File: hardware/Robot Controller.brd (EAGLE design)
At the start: 52.4 x 48.9 mm, 18 parts

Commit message: routing
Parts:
- moved R2 29.7 mm to (82.5, 59.7), turned to 0 degrees
- moved R1 5.85 mm to (82.5, 63.5), turned to 180 degrees
- moved R3 4.96 mm to (57.8, 49.5), turned to 0 degrees
- moved JP1 2.54 mm to (90.8, 43.2)
- moved SN74AHCU04N 1.42 mm to (55.9, 36.8)
- moved ATTINY 1.42 mm to (68.6, 40.6)
- moved JP3 1.27 mm to (55.9, 61.6)
- moved JP4 1.27 mm to (69.2, 61.6)
- moved JP6 1.27 mm to (47.0, 54.6)
- moved H1 1.27 mm to (47.0, 61.0)
- moved L293D 1.27 mm to (81.3, 38.1)
- moved LED1 1.27 mm to (60.3, 55.9)
- moved LED3 1.27 mm to (72.4, 55.9)
- moved S1 1.27 mm to (81.3, 53.3)
- moved LED2 0.63 mm to (48.3, 32.4)
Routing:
- net N$17: track 18.1 -> 74.1 mm, vias 0 -> 2
- net N$8: track 36.7 -> 71.3 mm, vias 0 -> 2
- net VCC: track 80.3 -> 113.3 mm, vias 0 -> 2
- net N$21: track 11.4 -> 36.4 mm, vias 0 -> 1
- net N$9: track 34.0 -> 55.9 mm, vias 0 -> 3
- net N$22: track 64.3 -> 80.9 mm, vias 0 -> 1
- net N$14: track 16.5 -> 32.2 mm, vias 2 -> 0
- net N$11: track 55.7 -> 46.0 mm, vias 3 -> 2
- net N$30: track 25.2 -> 34.5 mm
- net N$6: track 45.7 -> 53.4 mm, vias 0 -> 1
- net N$2: track 25.0 -> 31.6 mm, vias 0 -> 1
- net N$20: track 48.2 -> 54.3 mm, vias 1 -> 2
- net N$13: track 26.7 -> 32.3 mm, vias 1 -> 2
- net N$19: track 37.1 -> 32.0 mm
- net N$15: track 19.3 -> 24.3 mm
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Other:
- board size 52.4 x 48.9 mm -> 51.7 x 47.6 mm
- board text added: "1. A robot may not injure a human being or, through inaction, allow a human being to come to harm. 2. A robot must obey the orders given to it by human beings, except where such orders would conflict with the First Law. 3. A robot must protect its own existence as long as such p rotection does not conflict with the First or Second Laws."

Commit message: tighten up PCB
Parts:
- removed S1: (no value), switch-omron:B3F-10XX
- added JP7: (no value), pinhead:1X08
- JP8: device pinhead:1X10 -> pinhead:1X02
- moved JP2 36.1 mm to (79.4, 57.1), turned to 0 degrees
- moved JP8 34.7 mm to (77.5, 50.8), turned to 180 degrees
- moved R2 31.5 mm to (52.7, 49.5), turned to 90 degrees
- moved R1 29.5 mm to (56.5, 49.5), turned to 270 degrees
- moved H1 17.2 mm to (46.4, 43.8)
- moved JP3 9.38 mm to (47.6, 57.1)
- moved JP4 7.24 mm to (63.5, 57.1)
- moved JP6 3.86 mm to (46.4, 50.8), turned to 0 degrees
- moved LED1 3.59 mm to (57.8, 58.4), turned to 90 degrees
- moved JP5 2.84 mm to (78.7, 22.2)
- moved LED3 2.84 mm to (73.7, 58.4), turned to 90 degrees
- moved R3 2.54 mm to (60.3, 49.5), turned to 90 degrees
- moved JP1 2.54 mm to (90.8, 40.6)
- moved LED2 0.90 mm to (48.9, 33.0), turned to 90 degrees
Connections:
- net GND: now also JP8.2; no longer JP8.10, S1.2
- net N$23: now also JP7.8; no longer JP8.8
- net N$24: now also JP7.7; no longer JP8.7
- net N$25: now also JP7.6; no longer JP8.6
- net N$26: now also JP7.5; no longer JP8.5
- net N$27: now also JP7.4; no longer JP8.4
- net N$28: now also JP7.1; no longer JP8.1
- net N$29: now also JP7.2; no longer JP8.2
- net N$30: now also JP7.3; no longer JP8.3
- net N$31: now also JP8.1; no longer S1.3
- net VCC: no longer JP8.9
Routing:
- net N$8: track 71.3 -> 18.2 mm, vias 2 -> 0
- net N$17: track 74.1 -> 31.2 mm, vias 2 -> 0
- net N$22: track 80.9 -> 40.2 mm, vias 1 -> 2
- net VCC: track 113.3 -> 74.3 mm, vias 2 -> 1
- net N$9: track 55.9 -> 25.2 mm, vias 3 -> 0
- net N$3: track 35.2 -> 6.60 mm, vias 2 -> 0
- net N$21: track 36.4 -> 10.6 mm
- net N$20: track 54.3 -> 35.9 mm, vias 2 -> 0
- net N$19: track 32.0 -> 50.2 mm, vias 0 -> 2
- net GND: track 155.4 -> 139.8 mm, vias 4 -> 0
- net N$10: track 68.7 -> 54.3 mm, vias 2 -> 1
- net N$23: track 55.3 -> 42.7 mm, vias 2 -> 1
- net N$30: track 34.5 -> 23.8 mm
- net N$14: track 32.2 -> 21.8 mm
- net N$6: track 53.4 -> 43.1 mm, vias 1 -> 0
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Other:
- board size 51.7 x 47.6 mm -> 51.7 x 41.3 mm
- board text added: "L1"
- board text added: "RST"
- board text added: "robot core rev 0.1"
- board text removed: "1. A robot may not injure a human being or, through inaction, allow a human being to come to harm. 2. A robot must obey the orders given to it by human beings, except where such orders would conflict with the First Law. 3. A robot must protect its own existence as long as such p rotection does not conflict with the First or Second Laws."
- board text removed: "robot core"

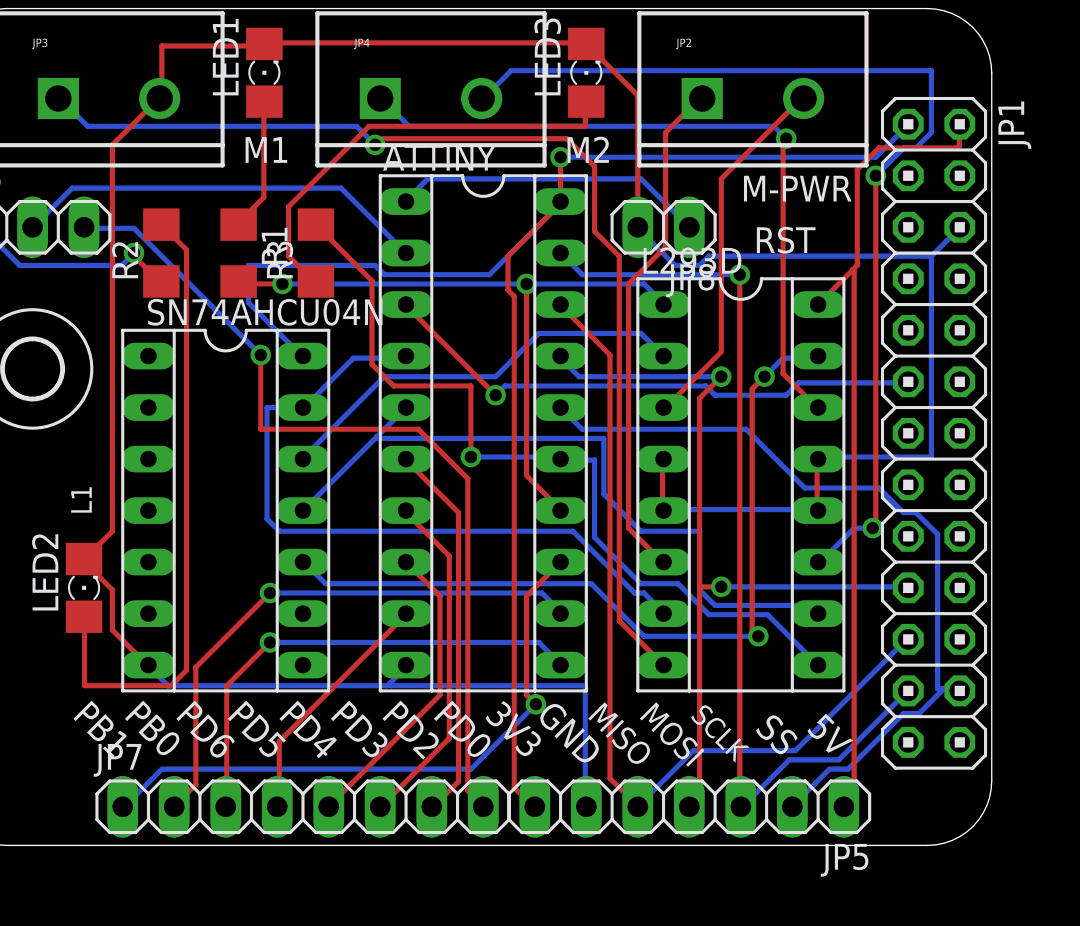
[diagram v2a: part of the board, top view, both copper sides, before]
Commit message: working on cleaning up schematic
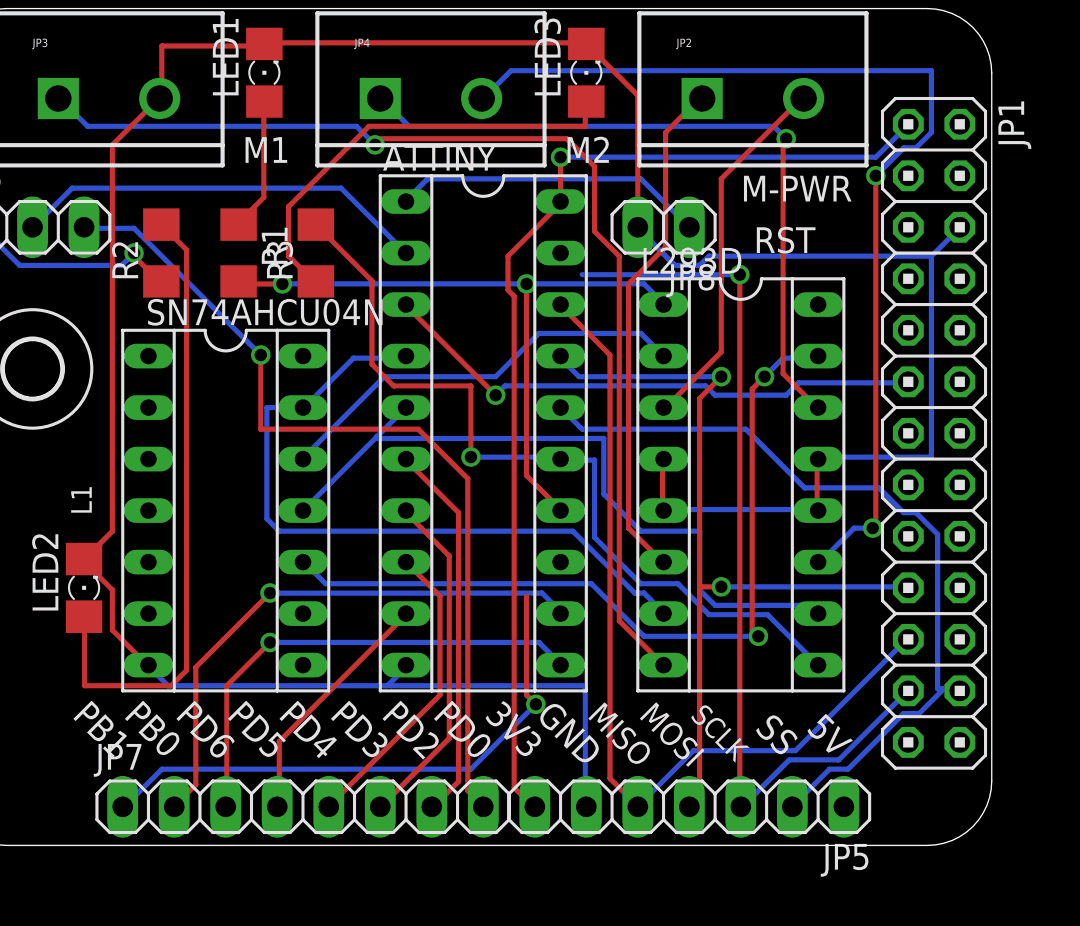
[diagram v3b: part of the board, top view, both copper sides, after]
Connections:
- net N$1 renamed M1PW'
- net N$11 renamed M2PW'
- net N$12 renamed 5V
- net N$28 renamed PB1'
- net N$29 renamed PB0'
- net N$30 renamed PD6'
- net N$31 renamed RESET'
- net N$5 renamed MOSI'
- net N$6 renamed MISO'
- net N$7 renamed SCL'
- net VCC renamed 3.3V
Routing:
- net 5V: track 40.8 -> 0.00 mm
- net 3.3V: track 74.3 -> 51.3 mm
- net PB1': track 30.4 -> 28.0 mm
- net SCL': track 46.2 -> 44.5 mm

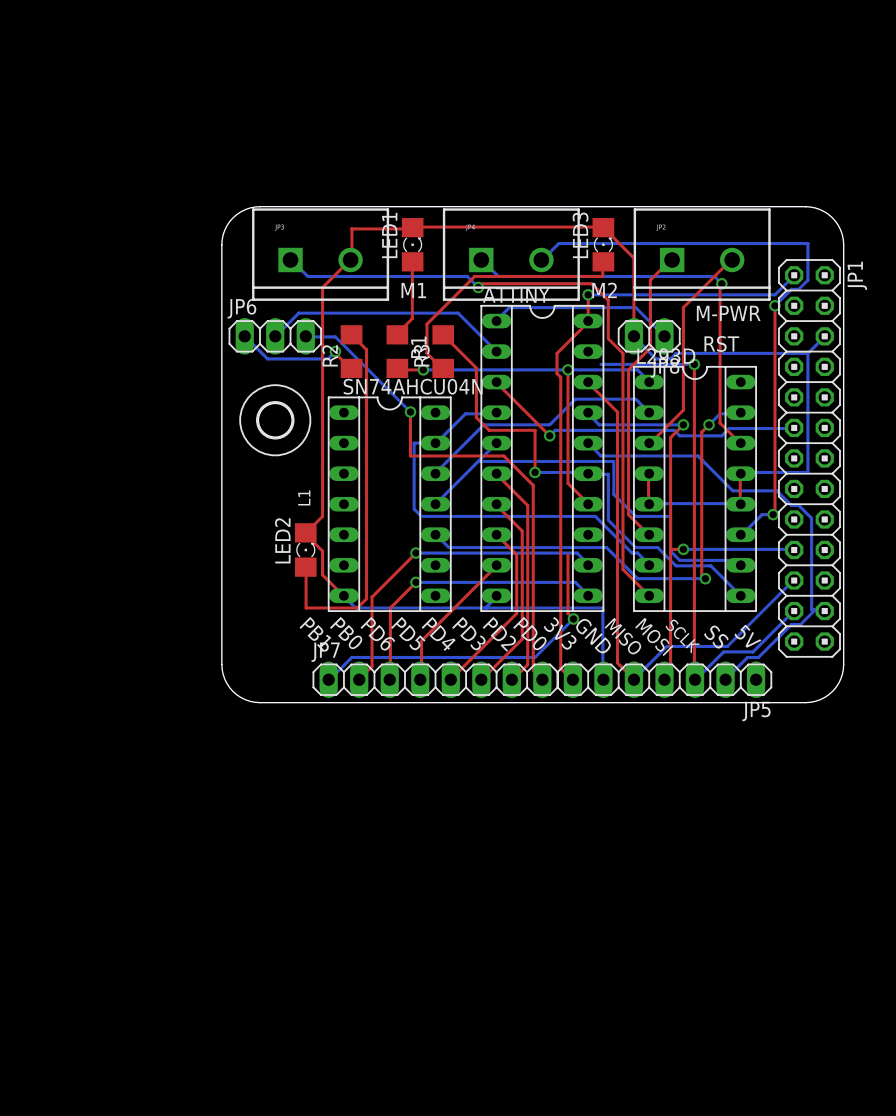
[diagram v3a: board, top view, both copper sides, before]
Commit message: need ADC, upgrading to ATmega328
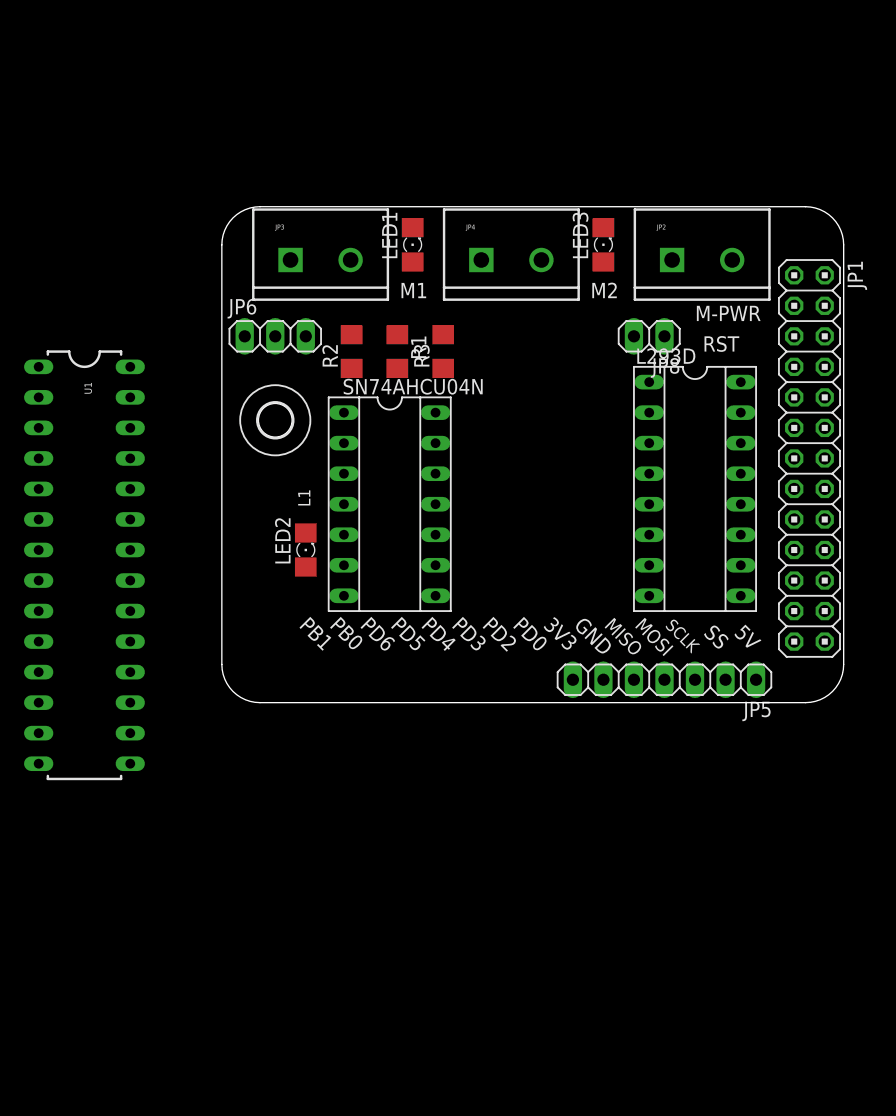
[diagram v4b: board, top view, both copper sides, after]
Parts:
- removed ATTINY: (no value), ic-package:SOCKET-20
- removed JP7: (no value), pinhead:1X08
- added U1: ATMEGA328P_PDIP, SparkFun-DigitalIC:DIL28-3
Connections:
- net N$15 renamed M1DR_'
- net N$22 renamed M2DR_'
- removed net N$13: ATTINY.4, L293D.7, SN74AHCU04N.13
- removed net N$16: ATTINY.2, JP6.2
- removed net N$2: ATTINY.3, JP1.11
- removed net N$20: ATTINY.5, L293D.10, SN74AHCU04N.11
- removed net N$24: ATTINY.6, JP7.7
- removed net N$25: ATTINY.7, JP7.6
- removed net N$26: ATTINY.8, JP7.5
- removed net N$27: ATTINY.9, JP7.4
- removed net N$4: ATTINY.16, JP1.24, JP5.2
- removed net PB0': ATTINY.12, JP7.2
- removed net PB1': ATTINY.13, JP7.1
- removed net PD6': ATTINY.11, JP7.3
- new net DEBUG': JP6.2, U1.2
- new net HOST': JP1.11, U1.3
- new net M1DR': L293D.7, SN74AHCU04N.13, U1.12
- new net M2DR': L293D.10, SN74AHCU04N.11, U1.13
- new net SS': JP1.24, JP5.2, U1.16
- net 3.3V: now also U1.7; no longer ATTINY.20
- net GND: now also U1.22, U1.8; no longer ATTINY.10
- net M1PW': now also U1.11; no longer ATTINY.14
- net M2PW': now also U1.5; no longer ATTINY.15
- net MISO': now also U1.18; no longer ATTINY.18
- net MOSI': now also U1.17; no longer ATTINY.17
- net N$23: no longer JP7.8
- net RESET': now also U1.1; no longer ATTINY.1
- net SCL': now also U1.19; no longer ATTINY.19
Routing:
- net GND: track 139.8 -> 0.00 mm
- net N$10: track 54.3 -> 0.00 mm, vias 1 -> 0
- net 3.3V: track 51.3 -> 0.00 mm, vias 1 -> 0
- net N$19: track 50.2 -> 0.00 mm, vias 2 -> 0
- net SCL': track 44.5 -> 0.00 mm, vias 1 -> 0
- net MISO': track 43.0 -> 0.00 mm
- net N$23: track 42.7 -> 0.00 mm, vias 1 -> 0
- net M2PW': track 40.5 -> 0.00 mm, vias 1 -> 0
- net MOSI': track 40.4 -> 0.00 mm, vias 2 -> 0
- net M2DR_': track 40.2 -> 0.00 mm, vias 2 -> 0
- net N$4: track 39.9 -> 0.00 mm
- net N$20: track 35.9 -> 0.00 mm
- net N$13: track 35.0 -> 0.00 mm
- net N$18: track 34.9 -> 0.00 mm, vias 1 -> 0
- net M1PW': track 33.2 -> 0.00 mm, vias 2 -> 0
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
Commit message: rough routing
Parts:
- moved U1 26.7 mm to (57.1, 33.7)
- moved SN74AHCU04N 13.3 mm to (69.2, 36.8)
- moved R2 12.7 mm to (65.4, 49.5)
- moved R1 12.1 mm to (68.6, 49.5)
- moved R3 11.4 mm to (71.8, 49.5)
- moved JP5 9.16 mm to (83.8, 14.6)
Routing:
- net GND: track 0.00 -> 147.9 mm
- net 3.3V: track 0.00 -> 78.2 mm
- net N$10: track 0.00 -> 77.9 mm
- net MISO': track 0.00 -> 58.7 mm
- net M2PW': track 0.00 -> 55.1 mm, vias 0 -> 2
- net HOST': track 0.00 -> 53.8 mm
- net 5V: track 0.00 -> 49.9 mm
- net M2DR': track 0.00 -> 49.8 mm
- net MOSI': track 0.00 -> 49.4 mm
- net SCL': track 0.00 -> 47.5 mm
- net N$18: track 0.00 -> 47.1 mm
- net SS': track 0.00 -> 44.7 mm
- net M1PW': track 0.00 -> 43.9 mm
- net N$19: track 0.00 -> 43.2 mm
- net M1DR': track 0.00 -> 43.2 mm
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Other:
- board size 51.7 x 41.3 mm -> 51.7 x 49.5 mm
- board text added: "robot core rev 0.2"
- board text removed: "PB0"
- board text removed: "PB1"
- board text removed: "PD0"
- board text removed: "PD2"
- board text removed: "PD3"
- board text removed: "PD4"
- board text removed: "PD5"
- board text removed: "PD6"
- board text removed: "robot core rev 0.1"

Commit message: WIP ATmega328 hardware
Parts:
- added JP7: (no value), pinhead:2X13
- moved JP5 37.3 mm to (49.5, 29.2)
- moved SN74AHCU04N 25.0 mm to (54.6, 57.1)
- moved L293D 18.5 mm to (71.8, 54.0), turned to 0 degrees
- moved H1 14.8 mm to (43.8, 58.4)
- moved JP6 14.8 mm to (43.8, 65.4)
- moved JP8 14.8 mm to (74.9, 65.4)
- moved LED1 14.8 mm to (55.2, 73.0)
- moved LED3 14.8 mm to (71.1, 73.0)
- moved R1 14.8 mm to (66.0, 64.1)
- moved R2 14.8 mm to (62.9, 64.1)
- moved R3 14.8 mm to (69.2, 64.1)
- moved JP1 14.8 mm to (88.3, 55.2)
- moved JP2 14.8 mm to (76.8, 71.8)
- moved JP3 14.8 mm to (45.1, 71.8)
- moved JP4 14.8 mm to (61.0, 71.8)
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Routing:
- net GND: track 147.9 -> 0.00 mm
- net 3.3V: track 78.2 -> 0.00 mm
- net N$10: track 77.9 -> 0.00 mm
- net MISO': track 58.7 -> 0.00 mm
- net M2PW': track 55.1 -> 0.00 mm, vias 2 -> 0
- net HOST': track 53.8 -> 0.00 mm
- net 5V: track 49.9 -> 0.00 mm
- net M2DR': track 49.8 -> 0.00 mm
- net MOSI': track 49.4 -> 0.00 mm
- net SCL': track 47.5 -> 0.00 mm
- net N$18: track 47.1 -> 0.00 mm
- net SS': track 44.7 -> 0.00 mm
- net M1PW': track 43.9 -> 0.00 mm
- net N$19: track 43.2 -> 0.00 mm
- net M1DR': track 43.2 -> 0.00 mm
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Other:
- board size 51.7 x 49.5 mm -> 51.7 x 73 mm

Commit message: update connections to match todays progress
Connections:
- net M1DR': now also U1.4; no longer U1.12
- net M1PW': now also U1.12; no longer U1.11
- net M2DR': now also U1.5; no longer U1.13
- net M2PW': no longer U1.5
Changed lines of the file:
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@@
 <contactref element="R1" pad="2"/>
 <contactref element="L293D" pad="1"/>
-<contactref element="U1" pad="11"/>
-<wire x1="66.04" y1="62.735" x2="62.865" y2="50.165" width="0" layer="19" extent="1-1"/>
-<wire x1="74.93" y1="38.1" x2="66.04" y2="62.735" width="0" layer="19" extent="1-1"/>
+<contactref element="U1" pad="12"/>
+<wire x1="62.865" y1="50.165" x2="66.04" y2="62.735" width="0" layer="19" extent="1-1"/>
+<wire x1="77.47" y1="38.1" x2="62.865" y2="50.165" width="0" layer="19" extent="1-1"/>
 </signal>
 <signal name="M2PW'">
 <contactref element="R3" pad="2"/>
 <contactref element="L293D" pad="9"/>
-<contactref element="U1" pad="5"/>
-<wire x1="59.69" y1="38.1" x2="69.215" y2="65.535" width="0" layer="19" extent="1-1"/>
-<wire x1="80.645" y1="57.785" x2="69.215" y2="65.535" width="0" layer="19" extent="1-1"/>
+<wire x1="69.215" y1="65.535" x2="80.645" y2="57.785" width="0" layer="19" extent="1-1"/>
 </signal>
 <signal name="M1DR'">
 <contactref element="SN74AHCU04N" pad="13"/>
 <contactref element="L293D" pad="7"/>
-<contactref element="U1" pad="12"/>
-<wire x1="78.105" y1="50.165" x2="58.42" y2="62.23" width="0" layer="19" extent="1-1"/>
-<wire x1="77.47" y1="38.1" x2="78.105" y2="50.165" width="0" layer="19" extent="1-1"/>
+<contactref element="U1" pad="4"/>
+<wire x1="58.42" y1="62.23" x2="78.105" y2="50.165" width="0" layer="19" extent="1-1"/>
+<wire x1="57.15" y1="38.1" x2="58.42" y2="62.23" width="0" layer="19" extent="1-1"/>
 </signal>
 <signal name="M2DR'">
 <contactref element="L293D" pad="10"/>
 <contactref element="SN74AHCU04N" pad="11"/>
-<contactref element="U1" pad="13"/>
+<contactref element="U1" pad="5"/>
 <wire x1="58.42" y1="57.15" x2="78.105" y2="57.785" width="0" layer="19" extent="1-1"/>
-<wire x1="80.01" y1="38.1" x2="58.42" y2="57.15" width="0" layer="19" extent="1-1"/>
+<wire x1="59.69" y1="38.1" x2="58.42" y2="57.15" width="0" layer="19" extent="1-1"/>
 </signal>
 <signal name="DEBUG'">

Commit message: WIP hardware
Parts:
- removed H1: MOUNT-HOLE2.8, holes:2,8
- JP7: device pinhead:2X13 -> pinhead:1X04
- moved JP8 50.8 mm to (38.2, 30.2), turned to 270 degrees
- moved JP5 43.7 mm to (89.7, 11.9), turned to 270 degrees
- moved L293D 43.4 mm to (62.6, 11.6), turned to 270 degrees
- moved JP6 41.8 mm to (38.2, 24.0), turned to 90 degrees
- moved R2 38.1 mm to (44.3, 30.9), turned to 270 degrees
- moved U1 24.8 mm to (74.9, 18.8), turned to 270 degrees
- moved R1 20.0 mm to (46.1, 63.0), turned to 0 degrees
- moved SN74AHCU04N 19.3 mm to (70.4, 46.0), turned to 0 degrees
- moved R3 6.93 mm to (62.4, 63.1), turned to 180 degrees
- moved LED1 6.47 mm to (50.7, 68.5)
- moved LED3 5.75 mm to (67.1, 69.0)
- moved JP3 5.49 mm to (40.5, 68.7)
- moved JP7 5.15 mm to (89.7, 25.9), turned to 90 degrees
- moved JP4 5.08 mm to (56.9, 68.7)
- moved JP2 5.08 mm to (72.8, 68.7)
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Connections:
- net DEBUG' renamed DEBUG
- removed net M2PW': L293D.9, R3.2
- new net ADC0: JP7.1, U1.23
- new net ADC1: JP7.2, U1.24
- new net ADC2: JP7.3, U1.25
- new net ADC3: JP7.4, U1.26
- new net M2PW: L293D.9, R3.2, U1.15
- net 3.3V: now also U1.20
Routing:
- net GND: track 0.00 -> 211.2 mm
- net 3.3V: track 0.00 -> 101.1 mm
- net N$10: track 0.00 -> 84.8 mm
- net N$9: track 0.00 -> 76.8 mm
- net 5V: track 0.00 -> 76.6 mm
- net M2PW: track 0.00 -> 75.7 mm
- net M1PW': track 0.00 -> 68.0 mm, vias 0 -> 1
- net N$19: track 0.00 -> 66.6 mm
- net N$8: track 0.00 -> 61.2 mm, vias 0 -> 1
- net N$18: track 0.00 -> 57.3 mm, vias 0 -> 1
- net MOSI': track 0.00 -> 55.6 mm
- net M1DR': track 0.00 -> 54.7 mm, vias 0 -> 1
- net MISO': track 0.00 -> 51.7 mm
- net SS': track 0.00 -> 50.6 mm
- net M2DR': track 0.00 -> 48.2 mm
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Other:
- board size 51.7 x 73 mm -> 56.2 x 85.1 mm
- board text added: "A0"
- board text added: "A1"
- board text added: "A2"
- board text added: "A3"
- board text added: "ANALOG"
- board text removed: ">"
